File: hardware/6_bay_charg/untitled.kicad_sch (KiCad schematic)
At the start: 14 parts, among them J1 Conn_01x02, U1 TVS1400DRV, U2 OKI-78SR-5_1.5-W36-C, U3 MCP1825S

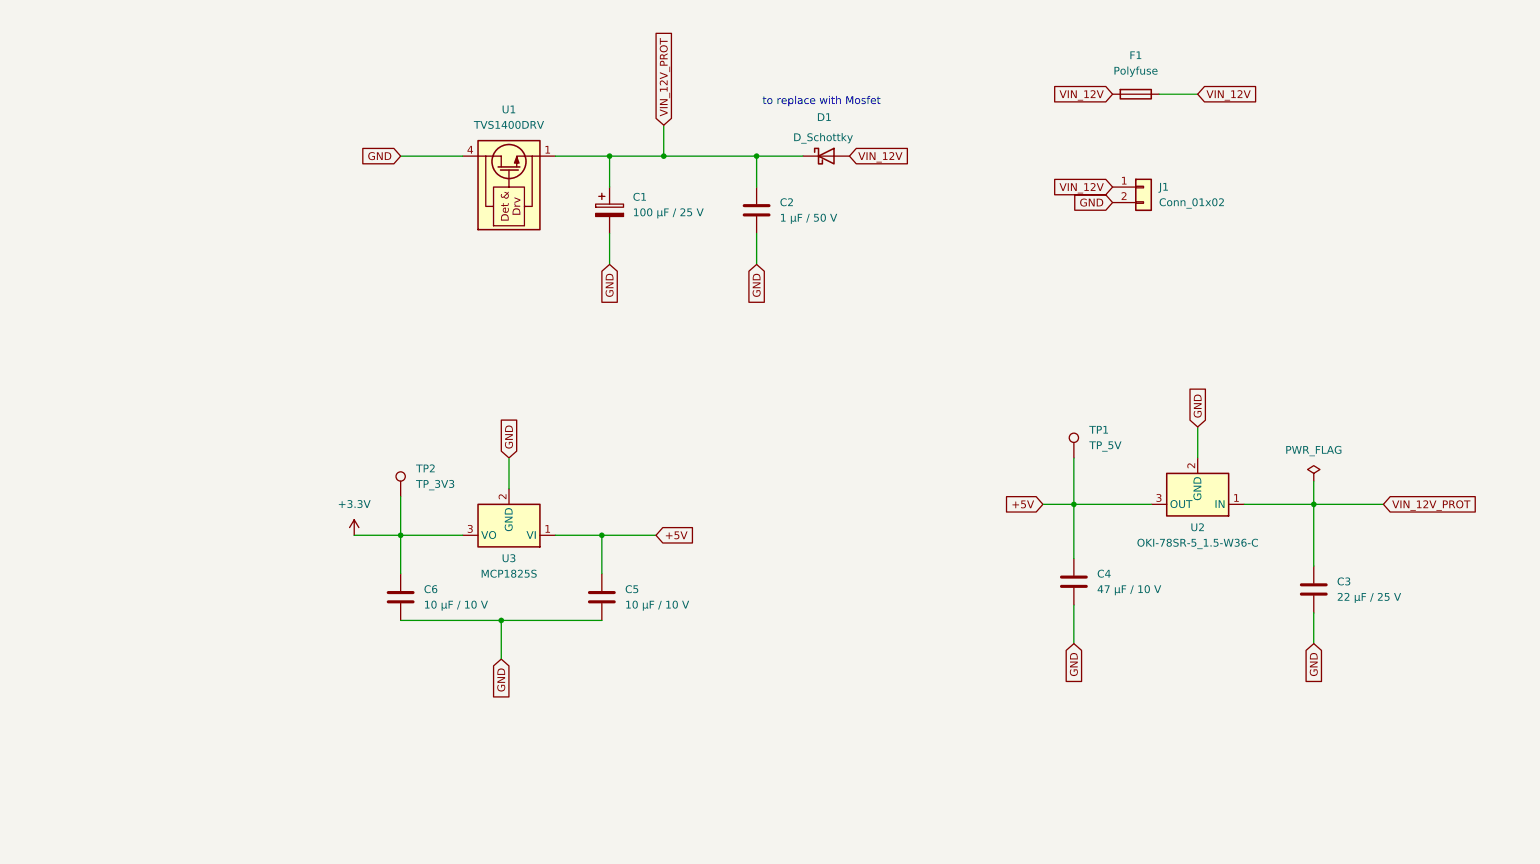
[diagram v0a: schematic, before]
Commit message: adding 3.3v buck sch + bay1
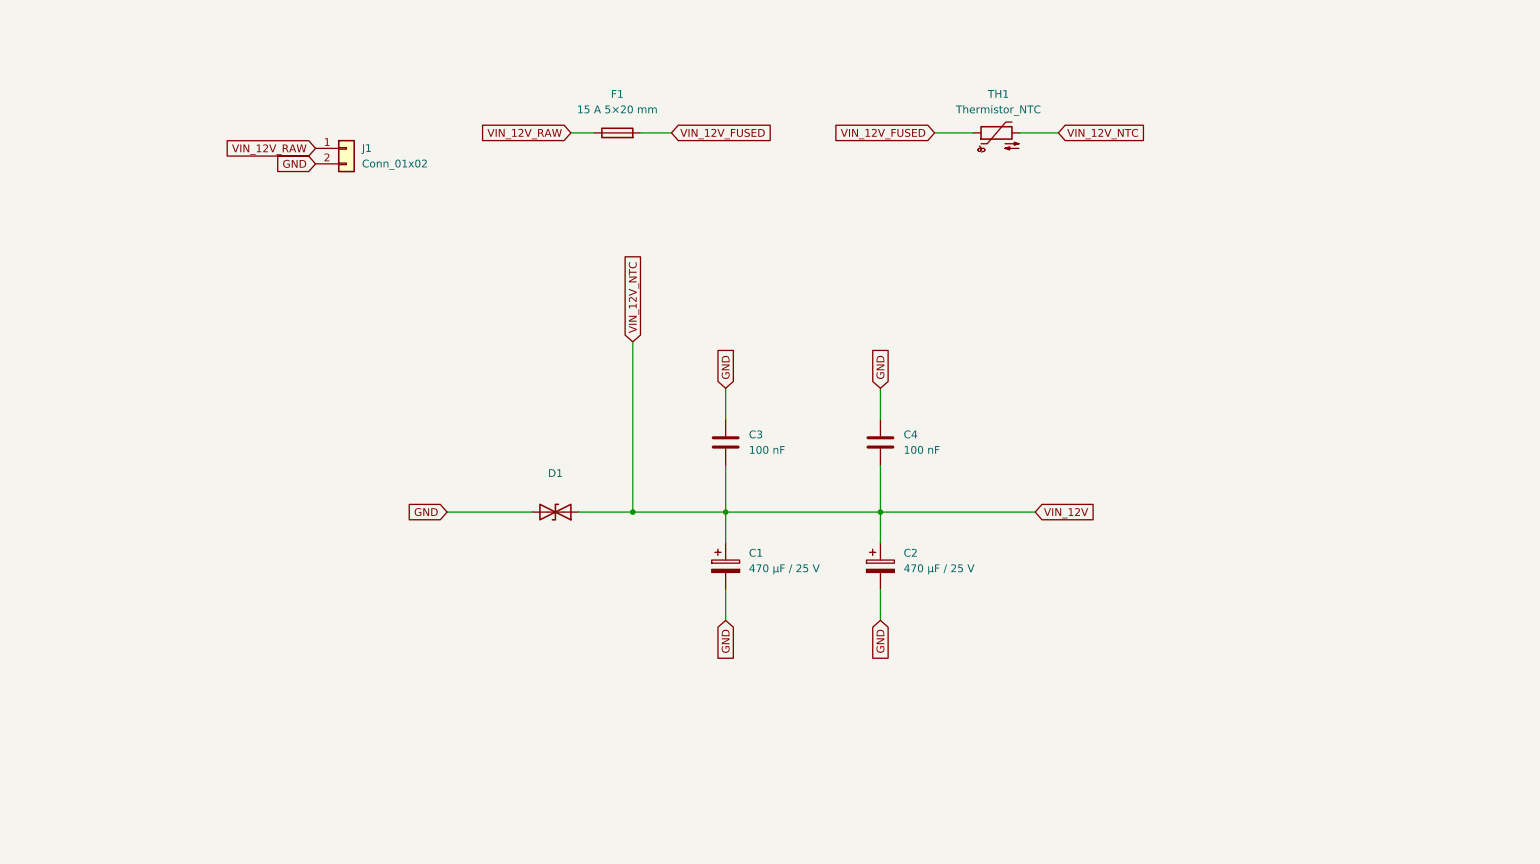
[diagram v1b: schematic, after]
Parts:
- removed C5, C6: 10 µF / 10 V, Capacitor_SMD:C_1206_3216Metric, symbol Device:C
- removed D1: D_Schottky, Diode_SMD:D_SMC, symbol Device:D_Schottky
- removed TP1: TP_5V, TestPoint:TestPoint_Pad_D1.5mm, symbol Connector:TestPoint
- removed TP2: TP_3V3, TestPoint:TestPoint_Pad_D1.5mm, symbol Connector:TestPoint
- removed U2: OKI-78SR-5_1.5-W36-C, Converter_DCDC:Converter_DCDC_Murata_OKI-78SR_Vertical, symbol Converter_DCDC:OKI-78SR-5_1.5-W36-C
- removed U3: MCP1825S, Package_TO_SOT_SMD:SOT-223-3_TabPin2, symbol Regulator_Linear:MCP1825S
- added TH1: Thermistor_NTC, symbol Device:Thermistor_NTC
- C1: value 100 µF / 25 V -> 470 µF / 25 V
- C2: value 1 µF / 50 V -> 470 µF / 25 V; symbol Device:C -> Device:C_Polarized
- C3: value 22 µF / 25 V -> 100 nF; footprint Capacitor_SMD:C_1210_3225Metric -> (none)
- C4: value 47 µF / 10 V -> 100 nF; footprint Capacitor_SMD:C_1210_3225Metric -> (none)
- D1: renamed from U1; value TVS1400DRV -> ~; footprint Package_SON:WSON-6-1EP_2x2mm_P0.65mm_EP1x1.6mm -> Diode_SMD:D_SMB; symbol Power_Protection:TVS1400DRV -> Device:D_TVS
- F1: value Polyfuse -> 15 A 5×20 mm; footprint Fuse:Fuse_Littelfuse-LVR100 -> (none)
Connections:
- net +5V is gone; now on net GND: C4.1
- net GND: now also C3.1, D1.2 (A2); no longer C3.2, C4.2, D1.4 (IN), D1.5 (IN), D1.6 (IN)
- net VIN_12V: now also C1.1, C2.1, C3.2, C4.2, D1.1 (A1), TH1.2; no longer F1.1, F1.2, J1.1 (Pin_1)
- removed net VIN_12V_PROT: C1.1, C2.1, C3.1, D1.1 (GND), D1.2 (GND), D1.3 (GND), D1.7 (GND)
- new net VIN_12V_FUSED: F1.2, TH1.1
- new net VIN_12V_RAW: F1.1, J1.1 (Pin_1)
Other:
- note removed: "to replace with Mosfet"
- company: (none) -> EOS Positioning Systems
- moved on the sheet: C1, J1

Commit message: Update KiCad schematics: dual GPIO charge/discharge per bay
- Refactored bay power control logic
- Separated GPIOs for charge and discharge paths
- Added safe idle state with hardware interlock
- Improved overall safety and control clarity
- Updated and exported schematic PDF plots
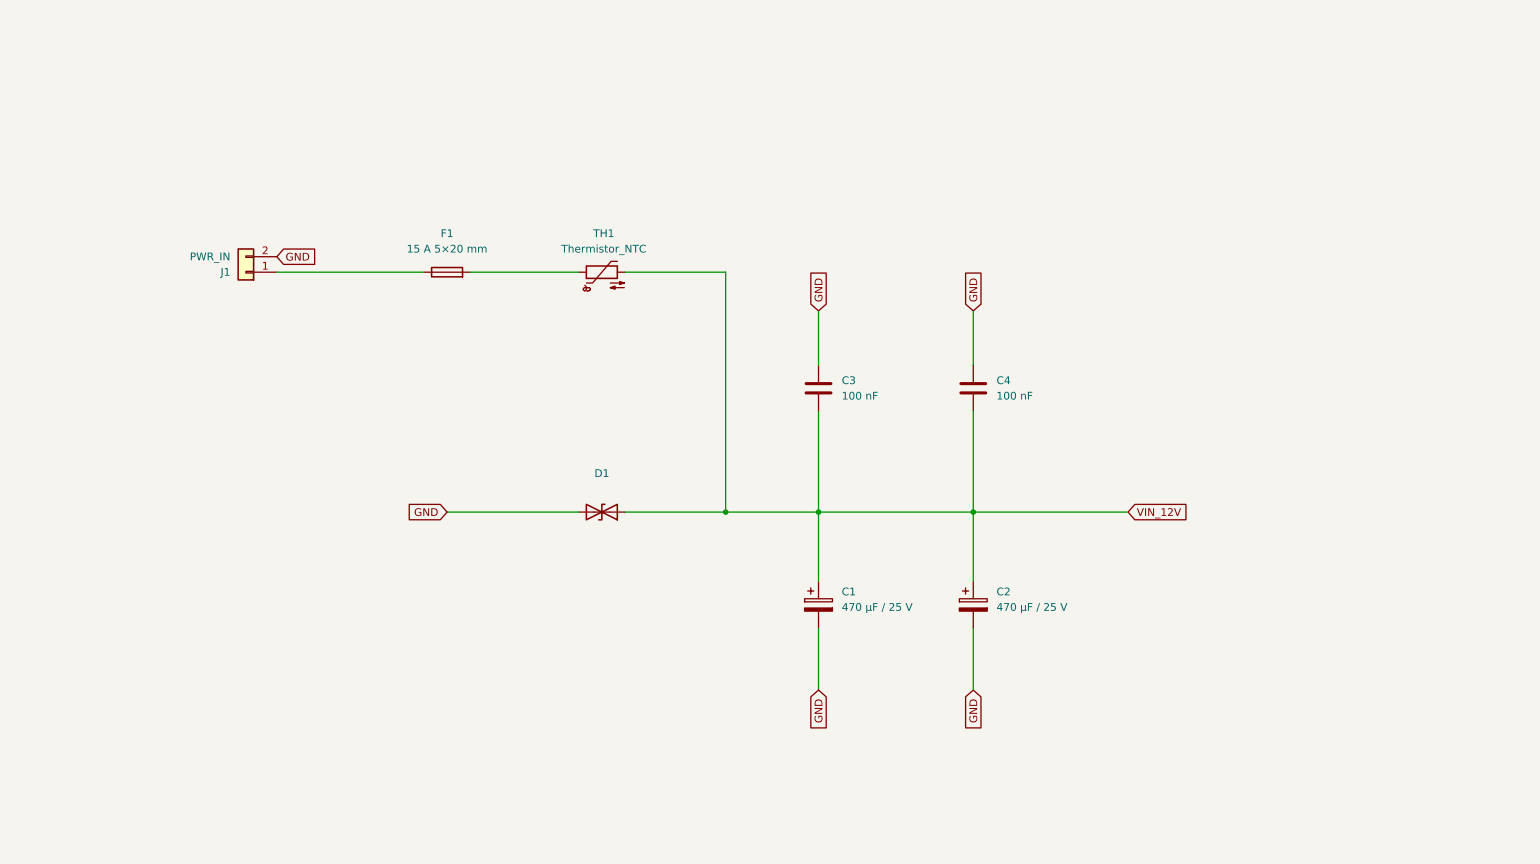
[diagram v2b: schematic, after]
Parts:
- J1: value Conn_01x02 -> PWR_IN
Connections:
- net VIN_12V_FUSED: no longer names the net of F1.2, TH1.1
- net VIN_12V_RAW: no longer names the net of F1.1, J1.1 (Pin_1)
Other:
- moved on the sheet: C1, C2, C3, C4, D1, F1, J1, TH1

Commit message: Integrate fan, USB interface, firmware, and cleaned KiCad schematics
- Added 12V fan for thermal management
- Integrated USB interface (hardware and firmware)
- Added initial firmware implementation
- Cleaned and refactored KiCad schematics
- Updated and regenerated schematic PDF plots
- Updated project README to reflect latest architecture
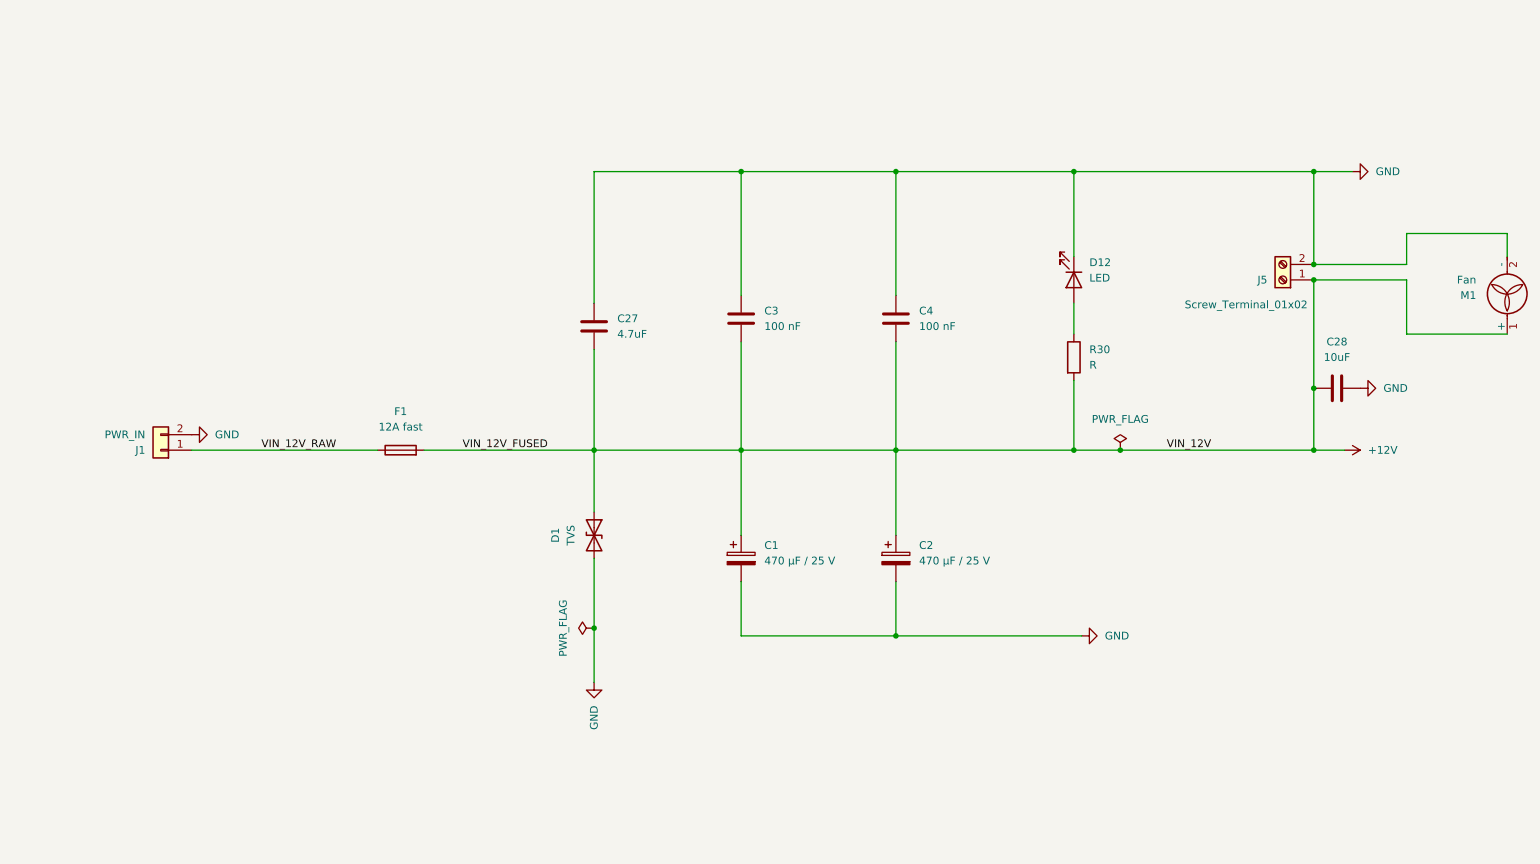
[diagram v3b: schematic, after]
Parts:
- removed TH1: Thermistor_NTC, symbol Device:Thermistor_NTC
- added C27: 4.7uF, symbol Device:C
- added C28: 10uF, symbol Device:C
- added D12: LED, symbol Device:LED
- added J5: Screw_Terminal_01x02, symbol Connector:Screw_Terminal_01x02
- added M1: Fan, symbol Motor:Fan
- added R30: R, symbol Device:R
- D1: value ~ -> TVS; footprint Diode_SMD:D_SMB -> Diode_SMD:D_SMA
- F1: value 15 A 5×20 mm -> 12A fast
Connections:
- net VIN_12V is gone; now on net +12V: C1.1, C2.1, C3.2, C4.2, D1.1 (A1)
- net GND: now also C27.1, C28.2, D12.1 (K), J5.2 (Pin_2), M1.2 (-)
- net VIN_12V_RAW: now reaches F1.1, J1.1 (Pin_1)
- net +12V: now reaches F1.2
- net +12V: now also C27.2, C28.1, J5.1 (Pin_1), M1.1 (+), R30.2
- new net: D12.2 (A), R30.1
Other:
- moved on the sheet: C1, C2, C3, C4, D1, F1, J1

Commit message: update_schematics
plot last updated pdf
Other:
- note added: "input power : 12V, 12A"
- note added: "power input 12V + Fan"
- title: Power (12 V → 5 V / 3.3 V) -> Power prot + Fan
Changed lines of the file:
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@@
 	(paper "A4")
 	(title_block
-		(title "Power (12 V → 5 V / 3.3 V)")
+		(title "Power prot + Fan")
 		(rev "Rev A")
 		(company "EOS Positioning Systems")
@@
 		(comment 3 "Drawn by: Takiyeddin Gherras")
 	)
+	(text "power input 12V + Fan"
+		(exclude_from_sim no)
+		(at 153.67 152.908 0)
+		(effects
+			(font
+				(size 3.27 3.27)
+				(thickness 0.4088)
+			)
+		)
+	)
+	(text "input power : 12V, 12A "
+		(exclude_from_sim no)
+		(at 45.212 77.724 0)
+		(effects
+			(font
+				(size 1.27 1.27)
+				(thickness 0.4088)
+			)
+		)
+	)
 	(junction
